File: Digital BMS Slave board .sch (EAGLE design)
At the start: 236 parts, among them J1 S4B-PH-K, J10 S3B-PH-K, J11 S6B-PH-K, J12 S4B-PH-K, J2 S4B-PH-K, J3 S4B-PH-K, J4 S6B-PH-K, J5 S2B-PH-K, J6 S2B-PH-K, J7 S2B-PH-K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

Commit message: Full routing 1.0ver. to review
DRC rules checked
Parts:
- removed J4: S6B-PH-K, con-jst-ph:S6B-PH-K
- removed TP13, TP65, TP66, TP67, TP68, TP69, TP70: TEST_PAD-[1.27MM], testing:TEST_PAD-[1.27MM]
- added J13: MOLEX22-12-406205-7068, commonly used connectors:MOLEX22-12-406205-7068
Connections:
- net CB0: no longer TP13.P$1
- net CB1: no longer TP70.P$1
- net CB2: no longer TP69.P$1
- net CB3: no longer TP68.P$1
- net CB4: no longer TP67.P$1
- net CB5: no longer TP66.P$1
- net CB6: no longer TP65.P$1
- net GND: now also J13-6.S; no longer J4.6
- net NFAULT: now also J13-5.S; no longer J4.5
- net RX1: now also J13-3.S; no longer J4.3
- net TX: now also J13-2.S; no longer J4.2
- net VIO: now also J13-4.S; no longer J4.1
- net WAKEUP: now also J13-1.S; no longer J4.4

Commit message: Ready to generte GERBER
Silkscreen+improvements
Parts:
- removed JP4: (no value), pinhead:PINHD-1X2
- removed TP1, TP10, TP11, TP12, TP15, TP16, TP17, TP2, TP3, TP4, TP5, TP6, TP7, TP8, TP9: TEST_PAD-[1MM], testing:TEST_PAD-[1MM]
- removed TP53, TP54, TP55, TP56, TP57, TP58, TP59, TP60, TP61, TP62, TP63, TP64: TEST_PAD-[1.27MM], testing:TEST_PAD-[1.27MM]
- added CHN, CHP, CLN, CLP, FHN, FHP, FLN, FLP, VC0, VC1, VC2, VC3, VC4, VC5, VC6: TEST_PAD-[1MM_SK], testing:TEST_PAD-[1MM_SK]
- added DR1, DR2, DR3, DR4, DR5, DR6, G1, G2, G3, G4, G5, G6: TEST_PAD-[1.27MM_SK], testing:TEST_PAD-[1.27MM_SK]
- JP1: device pinhead:PINHD-2X6 -> pinhead:PINHD-2X7
- RB1, RB2, RB3, RB4, RB5, RB6: device Resistors:R-EU2512 -> resistor:R-EU_R2512
- renumbered JP20 to SB1
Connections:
- removed net N$2: JP4.2, R6.2
- new net N$1: JP1.13, R6.2
- net COMH_N: now also CHN.P$1; no longer TP8.P$1
- net COMH_P: now also CHP.P$1; no longer TP15.P$1
- net COML_N: now also CLN.P$1; no longer TP1.P$1
- net COML_P: now also CLP.P$1; no longer TP5.P$1
- net FAULTH_N: now also FHN.P$1; no longer TP16.P$1
- net FAULTH_P: now also FHP.P$1; no longer TP17.P$1
- net FAULTL_N: now also FLN.P$1; no longer TP6.P$1
- net FAULTL_P: now also FLP.P$1; no longer TP7.P$1
- net N$22: now also DR3.P$1; no longer TP59.P$1
- net N$3: now also DR1.P$1; no longer TP62.P$1
- net N$30: now also G1.P$1; no longer TP53.P$1
- net N$31: now also DR2.P$1; no longer TP61.P$1
- net N$34: now also DR5.P$1; no longer TP64.P$1
- net N$60: now also G2.P$1; no longer TP54.P$1
- net N$62: now also G3.P$1; no longer TP55.P$1
- net N$63: now also DR4.P$1; no longer TP60.P$1
- net N$68: now also G4.P$1; no longer TP56.P$1
- net N$70: now also G5.P$1; no longer TP57.P$1
- net N$71: now also DR6.P$1; no longer TP63.P$1
- net N$76: now also G6.P$1; no longer TP58.P$1
- net VC0: now also VC0.P$1; no longer TP3.P$1
- net VC1: now also VC1.P$1; no longer TP2.P$1
- net VC2: now also VC2.P$1; no longer TP4.P$1
- net VC3: now also VC3.P$1; no longer TP9.P$1
- net VC4: now also VC4.P$1; no longer TP10.P$1
- net VC5: now also VC5.P$1; no longer TP11.P$1
- net VC6: now also VC6.P$1; no longer TP12.P$1
- net VPROG: now also JP1.14; no longer JP4.1
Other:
- note added: "Slave BMS is a part of Battery Management System, that measure battery module temperature, individual cells voltages, balanced them and transmit all information to MasterBMS"
- note added: "https://github.com/701lab/SlaveBMS"
- moved on the sheet: C12, C14, C15, C41, C42, C43, C44, C45, C46, C47, C48, C55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

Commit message: Some components names changed
BOM generated
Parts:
- removed J13: MOLEX22-12-406205-7068, commonly used connectors:MOLEX22-12-406205-7068
- added J4: S4B-PH-K, con-jst-ph:S4B-PH-K
- C3: value 2.2u/10V -> 2.2u/16V
- D13: value 6.2V -> GREEN; device Semiconductor_devices:SOD323-ZENER -> Semiconductor_devices:LED0805
- D9: value GREEN -> 6.2V; device Semiconductor_devices:LED0805 -> Semiconductor_devices:SOD323-ZENER
- J12: value S4B-PH-K -> MOLEX22-12-406205-7068; device con-jst-ph:S4B-PH-K -> commonly used connectors:MOLEX22-12-406205-7068
- R2, R74: value 100 -> 100, 0.25W
- renumbered JP6 to JP4, X5 to X1
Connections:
- net 4: now also J4.4; no longer J12.4
- net BAT1: now also J4.3; no longer J12.3
- net BAT3: now also J4.2; no longer J12.2
- net BAT5: now also J4.1; no longer J12.1
- net GND: now also D13.C, D9.A, J12-6.S; no longer D13.A, D9.C, J13-6.S
- net GPIO3: now also D9.C; no longer D13.C
- net N$28: now also D13.A; no longer D9.A
- net NFAULT: now also J12-5.S; no longer J13-5.S
- net RX1: now also J12-3.S; no longer J13-3.S
- net TX: now also J12-2.S; no longer J13-2.S
- net VIO: now also J12-4.S; no longer J13-4.S
- net WAKEUP: now also J12-1.S; no longer J13-1.S

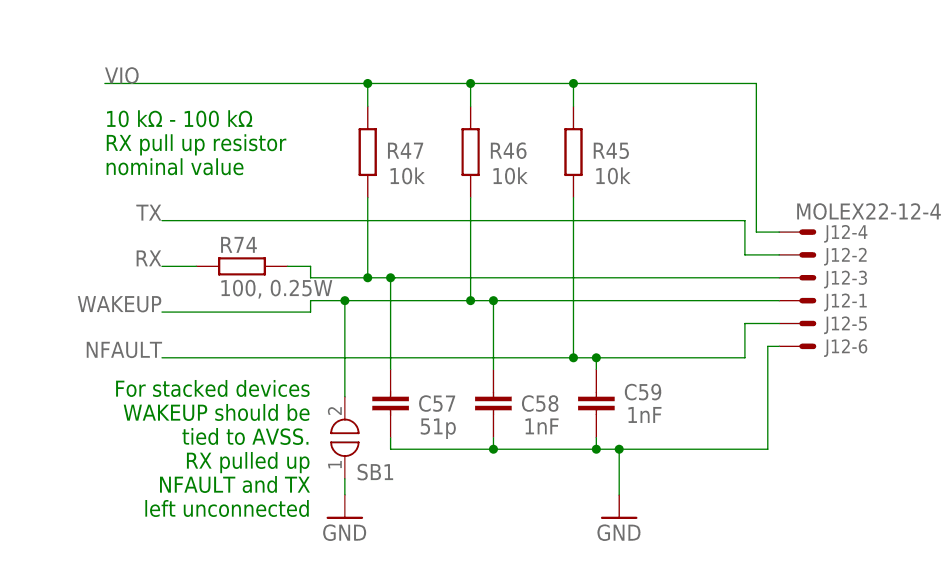
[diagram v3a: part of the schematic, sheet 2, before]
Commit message: communication fail correction
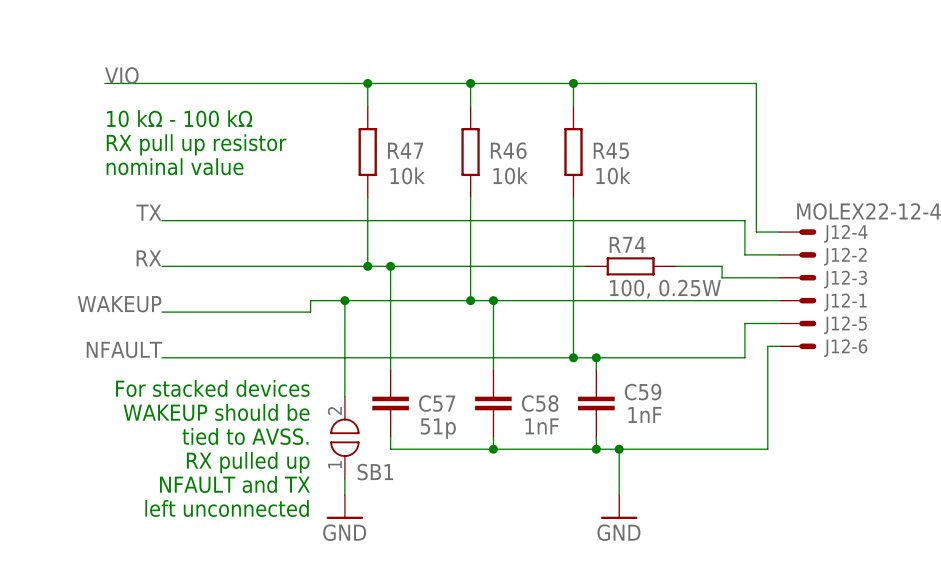
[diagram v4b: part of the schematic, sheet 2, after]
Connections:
- removed net RX1: C57.2, J12-3.S, R47.1, R74.1
- new net N$2: J12-3.S, R74.1
- net RX: now also C57.2, R47.1
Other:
- moved on the sheet: R74
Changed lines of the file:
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@@
 <setting verticaltext="up"/>
 </settings>
-<grid distance="0.1" unitdist="inch" unit="inch" style="lines" multiple="1" display="no" altdistance="0.01" altunitdist="inch" altunit="inch"/>
+<grid distance="0.05" unitdist="inch" unit="inch" style="lines" multiple="1" display="yes" altdistance="0.01" altunitdist="inch" altunit="inch"/>
 <layers>
 <layer number="1" name="Top" color="4" fill="1" visible="no" active="no"/>
@@
 </class>
 <class number="1" name="Power" width="0" drill="0">
+<clearance class="1" value="0.2032"/>
 </class>
 <class number="2" name="diff pairs" width="0" drill="0">
@@
 </segment>
 </net>
-<net name="VCC" class="0">
+<net name="VCC" class="1">
 <segment>
 <pinref part="C1" gate="G$1" pin="2"/>
@@
 <attribute name="VALUE" x="24.13" y="46.99" size="1.778" layer="96"/>
 </instance>
-<instance part="R74" gate="G$1" x="15.24" y="77.47" smashed="yes" rot="R180" grouprefs="UART_TO_ISO_COMMUNICATION1">
-<attribute name="NAME" x="12.7" y="78.9686" size="1.778" layer="95"/>
-<attribute name="VALUE" x="12.7" y="74.168" size="1.778" layer="96"/>
+<instance part="R74" gate="G$1" x="58.42" y="77.47" smashed="yes" rot="R180" grouprefs="UART_TO_ISO_COMMUNICATION1">
+<attribute name="NAME" x="55.88" y="78.9686" size="1.778" layer="95"/>
+<attribute name="VALUE" x="55.88" y="74.168" size="1.778" layer="96"/>
 </instance>
 <instance part="CLN" gate="G$1" x="-147.32" y="104.14" smashed="yes" rot="MR270">
@@
 </segment>
 </net>
-<net name="RX1" class="0">
-<segment>
-<pinref part="R47" gate="G$1" pin="1"/>
-<wire x1="31.75" y1="76.2" x2="29.21" y2="76.2" width="0.1524" layer="91" grouprefs="UART_TO_ISO_COMMUNICATION1"/>
-<wire x1="29.21" y1="85.09" x2="29.21" y2="76.2" width="0.1524" layer="91" grouprefs="UART_TO_ISO_COMMUNICATION1"/>
-<pinref part="C57" gate="G$1" pin="2"/>
-<wire x1="31.75" y1="66.04" x2="31.75" y2="76.2" width="0.1524" layer="91" grouprefs="UART_TO_ISO_COMMUNICATION1"/>
-<junction x="31.75" y="76.2" grouprefs="UART_TO_ISO_COMMUNICATION1"/>
-<wire x1="32.258" y1="76.2" x2="31.75" y2="76.2" width="0.1524" layer="91" grouprefs="UART_TO_ISO_COMMUNICATION1"/>
-<wire x1="74.93" y1="76.2" x2="31.75" y2="76.2" width="0.1524" layer="91" grouprefs="UART_TO_ISO_COMMUNICATION1"/>
-<pinref part="R74" gate="G$1" pin="1"/>
-<wire x1="20.32" y1="77.47" x2="22.86" y2="77.47" width="0.1524" layer="91" grouprefs="UART_TO_ISO_COMMUNICATION1"/>
-<wire x1="22.86" y1="77.47" x2="22.86" y2="76.2" width="0.1524" layer="91" grouprefs="UART_TO_ISO_COMMUNICATION1"/>
-<wire x1="22.86" y1="76.2" x2="29.21" y2="76.2" width="0.1524" layer="91" grouprefs="UART_TO_ISO_COMMUNICATION1"/>
-<junction x="29.21" y="76.2" grouprefs="UART_TO_ISO_COMMUNICATION1"/>
-<pinref part="J12" gate="-3" pin="S"/>
-</segment>
-</net>
 <net name="RX" class="0">
 <segment>
 <pinref part="R74" gate="G$1" pin="2"/>
-<wire x1="10.16" y1="77.47" x2="6.35" y2="77.47" width="0.1524" layer="91" grouprefs="UART_TO_ISO_COMMUNICATION1"/>
+<wire x1="53.34" y1="77.47" x2="31.75" y2="77.47" width="0.1524" layer="91" grouprefs="UART_TO_ISO_COMMUNICATION1"/>
 <label x="6.35" y="77.47" size="1.778" layer="95" rot="MR0" grouprefs="UART_TO_ISO_COMMUNICATION1"/>
+<pinref part="R47" gate="G$1" pin="1"/>
+<wire x1="31.75" y1="77.47" x2="29.21" y2="77.47" width="0.1524" layer="91" grouprefs="UART_TO_ISO_COMMUNICATION1"/>
+<wire x1="29.21" y1="77.47" x2="6.35" y2="77.47" width="0.1524" layer="91" grouprefs="UART_TO_ISO_COMMUNICATION1"/>
+<wire x1="29.21" y1="85.09" x2="29.21" y2="77.47" width="0.1524" layer="91"/>
+<junction x="29.21" y="77.47"/>
+<pinref part="C57" gate="G$1" pin="2"/>
+<wire x1="31.75" y1="66.04" x2="31.75" y2="77.47" width="0.1524" layer="91" grouprefs="UART_TO_ISO_COMMUNICATION1"/>
+<junction x="31.75" y="77.47"/>
 </segment>
 </net>
@@
 </segment>
 </net>
+<net name="N$2" class="0">
+<segment>
+<pinref part="R74" gate="G$1" pin="1"/>
+<wire x1="63.5" y1="77.47" x2="68.58" y2="77.47" width="0.1524" layer="91"/>
+<wire x1="68.58" y1="77.47" x2="68.58" y2="76.2" width="0.1524" layer="91"/>
+<pinref part="J12" gate="-3" pin="S"/>
+<wire x1="68.58" y1="76.2" x2="74.93" y2="76.2" width="0.1524" layer="91"/>
+</segment>
+</net>

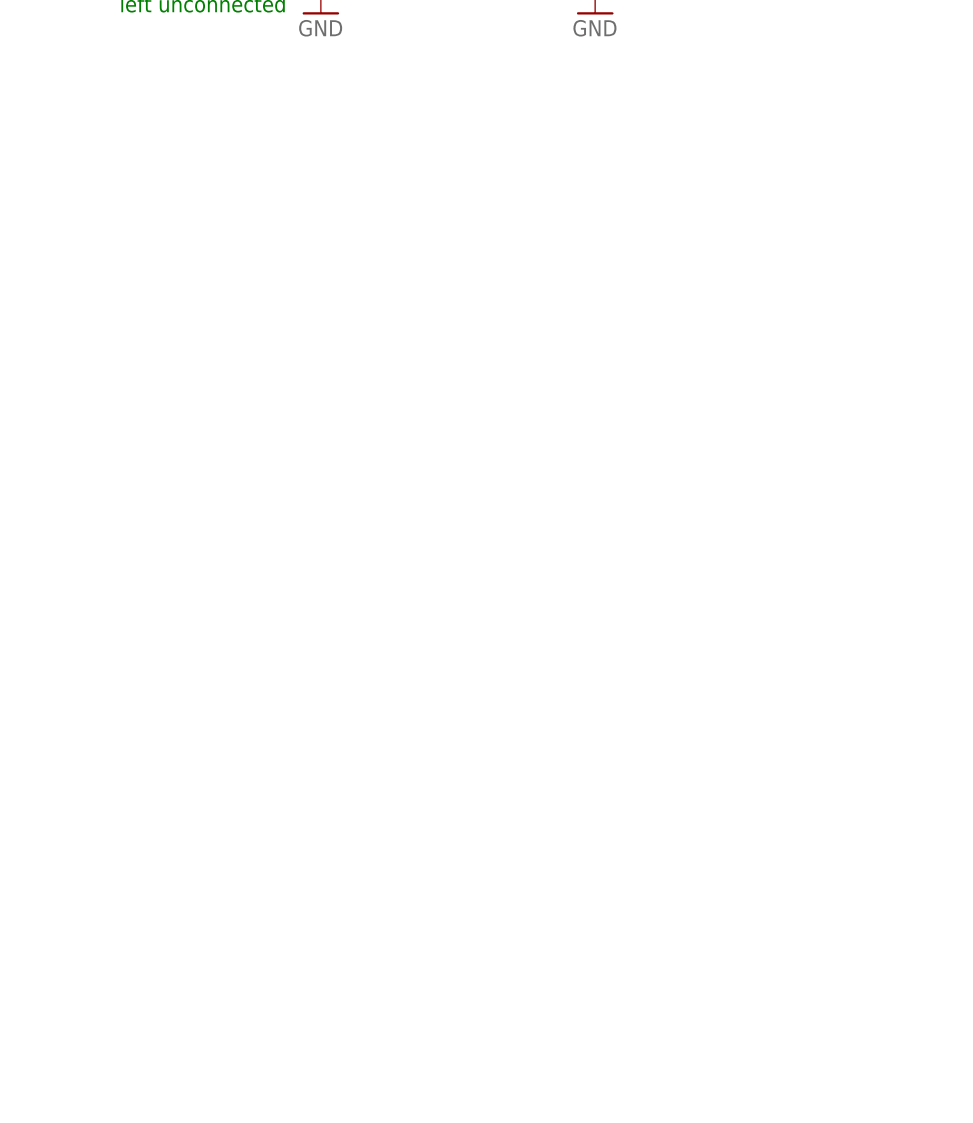
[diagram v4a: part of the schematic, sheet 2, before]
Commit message: Resistor ladder added as a panel
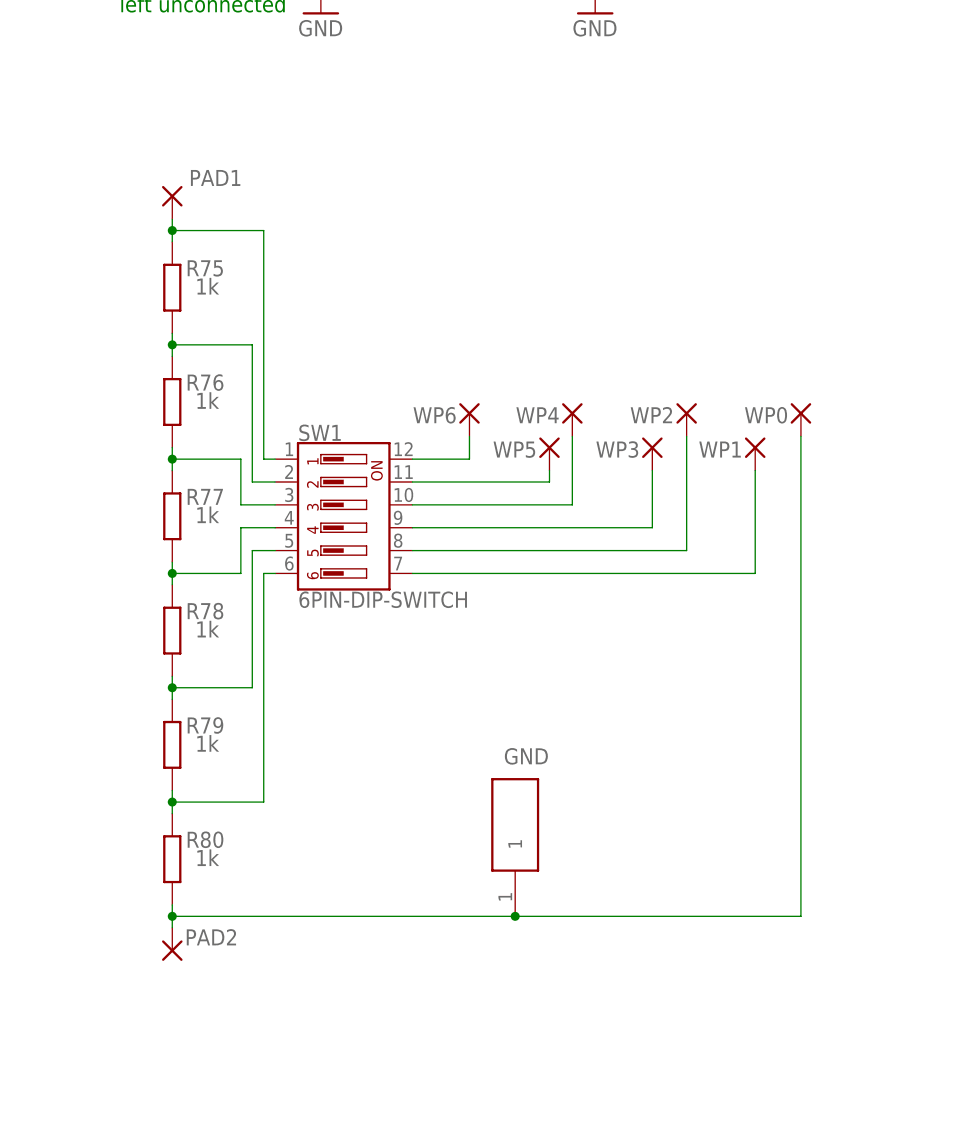
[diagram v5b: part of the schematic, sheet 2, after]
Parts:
- added GND: 5000, testing:5000
- added P1, P2: TEST_PAD-[1MM_SK], testing:TEST_PAD-[1MM_SK]
- added P3, P4, P8, P9: TEST_PAD-[1.27MM_SK], testing:TEST_PAD-[1.27MM_SK]
- added PAD1, PAD2: (no value), testing:SMD_PAD
- added R75, R76, R77, R78, R79, R80: 1k, Resistors:R-EU0603
- added SW1: 6PIN-DIP-SWITCH, buttons and switches:6PIN-DIP-SWITCH
- added WP0, WP1, WP2, WP3, WP4, WP5, WP6: (no value), wirepad:2,54/1,1
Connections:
- new net N$10: PAD1.P, R75.1, SW1.1
- new net N$11: GND.1, PAD2.P, R80.2, WP0.P
- new net N$13: R79.2, R80.1, SW1.6
- new net N$14: R78.2, R79.1, SW1.5
- new net N$15: SW1.9, WP3.P
- new net N$16: SW1.8, WP2.P
- new net N$17: SW1.7, WP1.P
- new net N$4: SW1.12, WP6.P
- new net N$5: SW1.11, WP5.P
- new net N$6: R77.2, R78.1, SW1.4
- new net N$7: SW1.10, WP4.P
- new net N$8: R76.2, R77.1, SW1.3
- new net N$9: R75.2, R76.1, SW1.2
- net AVDD: now also P4.P$1
- net BAT: now also P1.P$1
- net GND: now also P8.P$1, P9.P$1
- net REF1: now also P2.P$1
- net VIO: now also P3.P$1
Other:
- moved on the sheet: C10

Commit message: changes for testing puposes
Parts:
- removed P3, P9: TEST_PAD-[1.27MM_SK], testing:TEST_PAD-[1.27MM_SK]
- removed SB1: SOLDER_BRIDGE, testing:SOLDER_BRIDGE
- added JP5: (no value), pinhead:PINHD-2X3
- added VLDO: TEST_PAD-[1.27MM_SK], testing:TEST_PAD-[1.27MM_SK]
- WP0, WP1, WP2, WP3, WP4, WP5, WP6: device wirepad:2,54/1,1 -> commonly used connectors:WIRE_TO_BOARD_2,54/1,1
- renumbered P1 to BAT, P2 to REF, P4 to AVDD, P8 to VSS
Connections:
- new net 125: C58.2, JP5.2, R46.1
- new net SYS_RAIL: J12-4.S, JP5.1, R45.2, R46.2, R47.2
- new net VLDO: C7.1, C9.1, JP5.5, U1.CVDD, U1.VLDO, VLDO.P$1
- net GND: now also JP5.6; no longer P9.P$1, SB1.1
- net N$1: now also C12.1; no longer R6.2
- net VIO: now also JP5.3; no longer C7.1, C9.1, J12-4.S, P3.P$1, R45.2, R46.2, R47.2, U1.CVDD, U1.VLDO
- net VPROG: now also R6.2; no longer C12.1
- net WAKEUP: now also JP5.4; no longer C58.2, R46.1, SB1.2
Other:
- note added: "For BASE device connect VIO to SYS_RAIL For STACK device to CVDD 5V signal"
- moved on the sheet: C10, C11, C12, C2, C57, C58, C59, C7, C9, R1, R47, R6

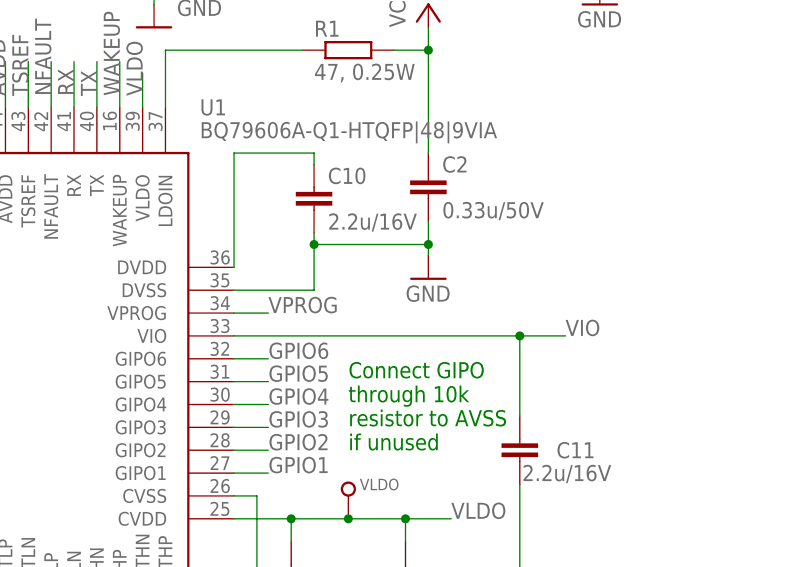
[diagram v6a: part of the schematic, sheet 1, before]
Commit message: VPROG pads added
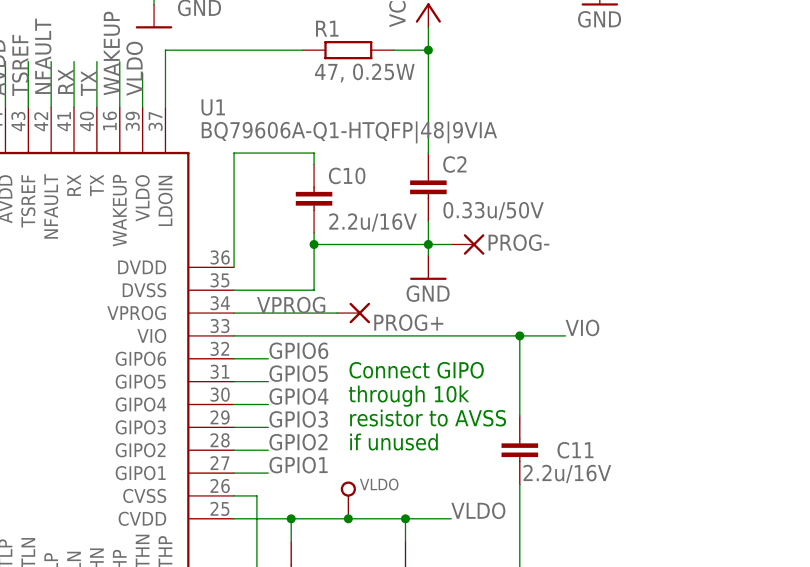
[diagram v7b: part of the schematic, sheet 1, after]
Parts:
- added PROG+, PROG-: (no value), testing:SMD_PAD
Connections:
- net GND: now also PROG-.P
- net VPROG: now also PROG+.P
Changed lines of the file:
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@@
 <part name="C11" library="resistor" library_urn="urn:adsk.eagle:library:348" deviceset="C-EU" device="C0603" package3d_urn="urn:adsk.eagle:package:23616/2" value="2.2u/16V"/>
 <part name="JP5" library="pinhead" library_urn="urn:adsk.eagle:library:325" deviceset="PINHD-2X3" device="" package3d_urn="urn:adsk.eagle:package:22462/2"/>
+<part name="PROG+" library="testing" library_urn="urn:adsk.eagle:library:13096589" deviceset="SMD_PAD" device="" package3d_urn="urn:adsk.eagle:package:16041846/4"/>
+<part name="PROG-" library="testing" library_urn="urn:adsk.eagle:library:13096589" deviceset="SMD_PAD" device="" package3d_urn="urn:adsk.eagle:package:16041846/4"/>
 </parts>
 <sheets>
@@
 <attribute name="VALUE" x="180.594" y="9.271" size="1.778" layer="96"/>
 </instance>
+<instance part="PROG+" gate="1" x="162.56" y="27.94" smashed="yes" rot="R180">
+<attribute name="NAME" x="163.957" y="25.9842" size="1.778" layer="95"/>
+<attribute name="VALUE" x="163.703" y="31.242" size="1.778" layer="96" rot="R180"/>
+</instance>
+<instance part="PROG-" gate="1" x="175.26" y="35.56" smashed="yes" rot="R180">
+<attribute name="NAME" x="176.657" y="34.8742" size="1.778" layer="95"/>
+<attribute name="VALUE" x="176.403" y="38.862" size="1.778" layer="96" rot="R180"/>
+</instance>
 </instances>
 <busses>
@@
 <wire x1="148.59" y1="30.48" x2="157.48" y2="30.48" width="0.1524" layer="91"/>
 <wire x1="157.48" y1="30.48" x2="157.48" y2="35.56" width="0.1524" layer="91"/>
+<pinref part="PROG-" gate="1" pin="P"/>
+<wire x1="172.72" y1="35.56" x2="170.18" y2="35.56" width="0.1524" layer="91"/>
 </segment>
 <segment>
@@
 <segment>
 <pinref part="U1" gate="G$1" pin="VPROG"/>
-<wire x1="148.59" y1="27.94" x2="152.4" y2="27.94" width="0.1524" layer="91"/>
-<label x="152.4" y="27.94" size="1.778" layer="95"/>
-</segment>
-<segment>
+<wire x1="148.59" y1="27.94" x2="160.02" y2="27.94" width="0.1524" layer="91"/>
+<label x="151.13" y="27.94" size="1.778" layer="95"/>
+<pinref part="PROG+" gate="1" pin="P"/>
+</segment>
+<segment>
